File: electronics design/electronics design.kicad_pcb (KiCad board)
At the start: 2 copper layers, 70 x 96 mm, 25 parts, among them SW1 SW_Push, SW10 RotaryEncoder_Switch, SW2 SW_Push, SW3 SW_Push, SW4 SW_Push, SW5 SW_Push, SW6 SW_Push, SW7 SW_Push, SW8 SW_Push, SW9 SW_Push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

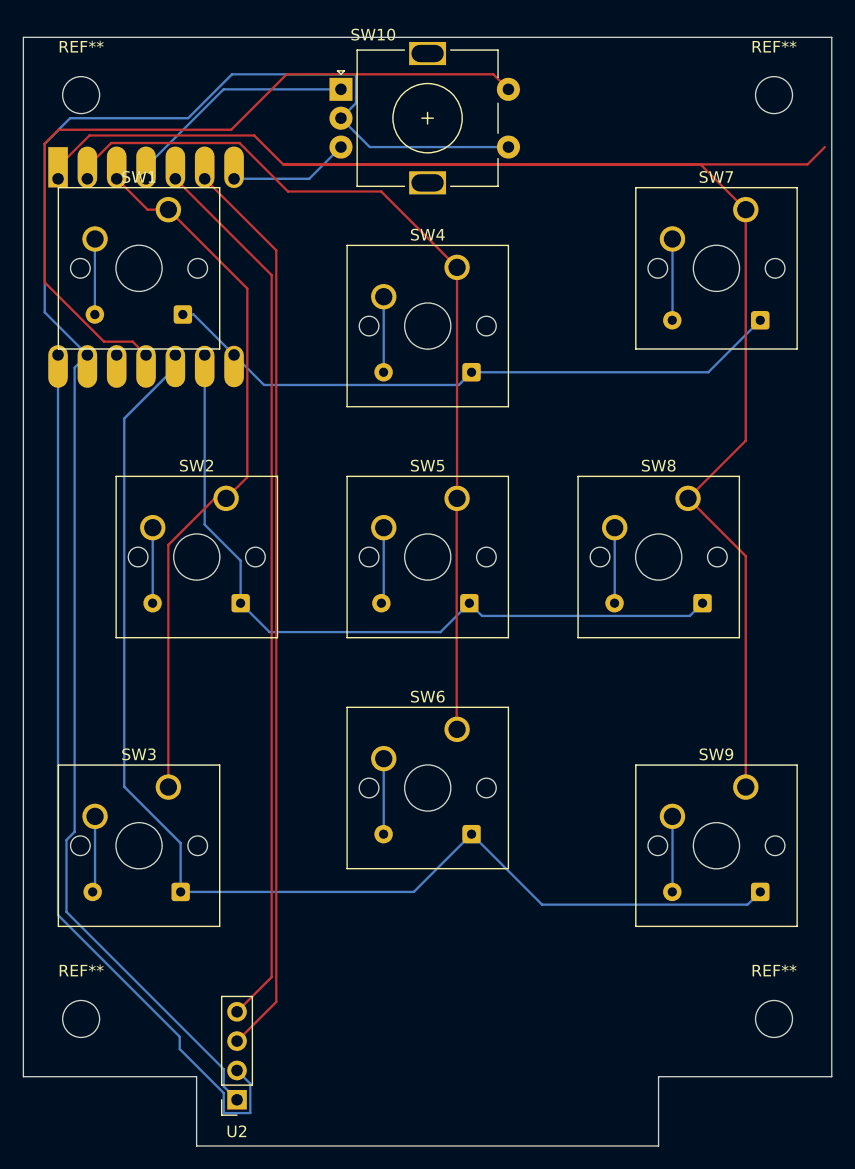
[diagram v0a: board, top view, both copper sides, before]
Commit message: Changed the position of the diodes to make space for the buttons.
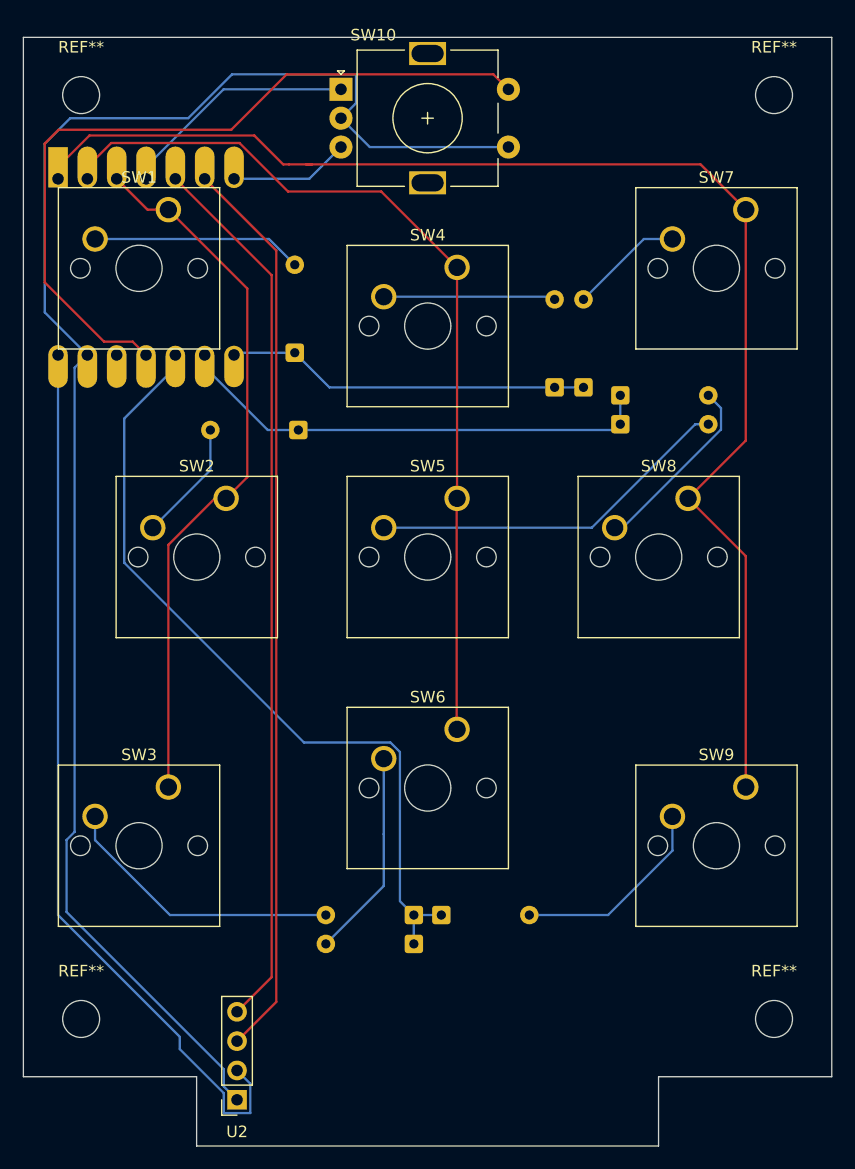
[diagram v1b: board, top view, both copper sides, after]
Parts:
- moved D9 27.7 mm to (116.2, 131.0), turned to 0 degrees
- moved D3 20.3 mm to (113.8, 131.0)
- moved D7 20.3 mm to (131.7, 88.5), turned to 0 degrees
- moved D6 19.4 mm to (131.7, 86.0), turned to 0 degrees
- moved D5 16.4 mm to (128.5, 85.3), turned to 90 degrees
- moved D2 15.8 mm to (103.8, 89.0)
- moved D8 10.7 mm to (113.8, 133.5)
- moved D1 10.2 mm to (103.5, 82.3), turned to 90 degrees
- moved D4 7.31 mm to (126.0, 85.3), turned to 90 degrees
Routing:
- net Net-(U1-PA02_A0_D0): track 166.5 -> 119.0 mm
- net Net-(D3-K): track 105.6 -> 70.0 mm
- net Net-(D7-A): track 6.62 -> 31.8 mm
- net Net-(D2-K): track 65.8 -> 42.0 mm
- net Net-(D1-K): track 54.8 -> 31.6 mm
- net Net-(D3-A): track 6.62 -> 24.7 mm
- net Net-(D1-A): track 6.55 -> 18.2 mm
- net Net-(D8-A): track 6.55 -> 18.1 mm
- net Net-(D9-A): track 6.55 -> 17.7 mm
- net Net-(D6-A): track 6.55 -> 16.1 mm
- net Net-(D4-A): track 6.55 -> 14.9 mm
- net Net-(D2-A): track 6.55 -> 10.5 mm
- net Net-(D5-A): track 7.05 -> 9.87 mm
